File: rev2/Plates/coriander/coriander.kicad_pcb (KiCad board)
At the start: 2 copper layers, 242.9 x 88.2 mm, 44 parts

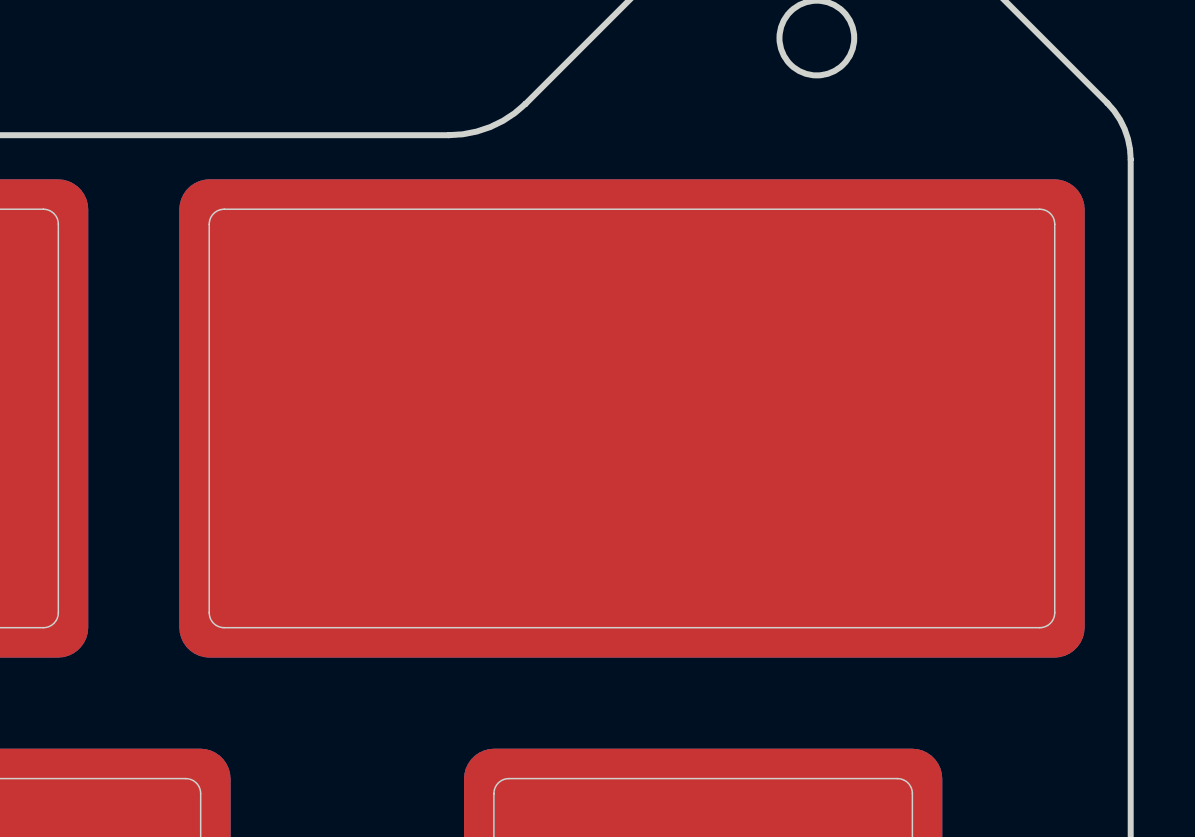
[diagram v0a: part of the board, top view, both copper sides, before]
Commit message: Fix plate encoder cutouts
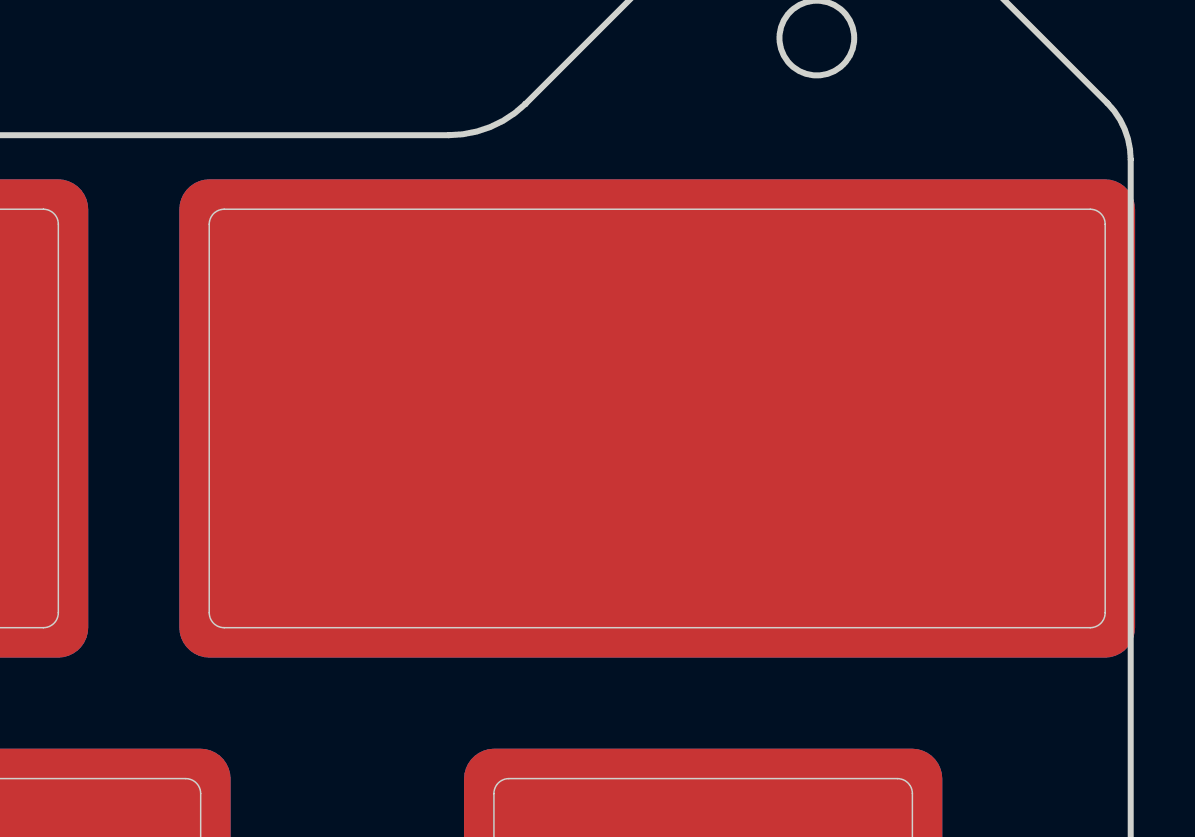
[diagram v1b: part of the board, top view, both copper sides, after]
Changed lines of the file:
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@@
     (visible_elements 7FFFEFFF)
     (pcbplotparams
-      (layerselection 0x01000_7ffffffe)
+      (layerselection 0x010c0_ffffffff)
       (usegerberextensions false)
       (usegerberattributes false)
@@
       (padsonsilk false)
       (subtractmaskfromsilk false)
-      (outputformat 3)
+      (outputformat 1)
       (mirror false)
       (drillshape 0)
@@
     (fp_line (start -16.66875 9.525) (end -16.66875 -9.525) (layer Dwgs.User) (width 0.15))
     (fp_line (start -16.66875 -9.525) (end 16.66875 -9.525) (layer Dwgs.User) (width 0.15))
-    (fp_line (start 13.64375 -7) (end -13.64375 -7) (layer Edge.Cuts) (width 0.05))
+    (fp_line (start 15.33125 -7) (end -13.64375 -7) (layer Edge.Cuts) (width 0.05))
     (fp_line (start -14.14375 -6.5) (end -14.14375 6.5) (layer Edge.Cuts) (width 0.05))
-    (fp_line (start -13.64375 7) (end 13.64375 7) (layer Edge.Cuts) (width 0.05))
-    (fp_line (start 14.14375 6.5) (end 14.14375 -6.5) (layer Edge.Cuts) (width 0.05))
-    (fp_arc (start 13.64375 -6.5) (end 14.14375 -6.5) (angle -90) (layer Edge.Cuts) (width 0.05))
+    (fp_line (start -13.64375 7) (end 15.33125 7) (layer Edge.Cuts) (width 0.05))
+    (fp_line (start 15.83125 6.5) (end 15.83125 -6.5) (layer Edge.Cuts) (width 0.05))
+    (fp_arc (start 15.33125 -6.5) (end 15.83125 -6.5) (angle -90) (layer Edge.Cuts) (width 0.05))
     (fp_arc (start -13.64375 -6.5) (end -13.64375 -7) (angle -90) (layer Edge.Cuts) (width 0.05))
     (fp_arc (start -13.64375 6.5) (end -14.14375 6.5) (angle -90) (layer Edge.Cuts) (width 0.05))
-    (fp_arc (start 13.64375 6.5) (end 13.64375 7) (angle -90) (layer Edge.Cuts) (width 0.05))
-    (pad 1 smd roundrect (at 0 0 180) (size 30.2875 16) (layers F.Cu F.Mask) (roundrect_rratio 0.063))
-    (pad 1 smd roundrect (at 0 0 180) (size 30.2875 16) (layers B.Cu B.Mask) (roundrect_rratio 0.063))
+    (fp_arc (start 15.33125 6.5) (end 15.33125 7) (angle -90) (layer Edge.Cuts) (width 0.05))
+    (pad 1 smd roundrect (at 0.84375 0 180) (size 31.975 16) (layers F.Cu F.Mask) (roundrect_rratio 0.063))
+    (pad 1 smd roundrect (at 0.84375 0 180) (size 31.975 16) (layers B.Cu B.Mask) (roundrect_rratio 0.063))
   )
   (module Keybage_MX_Cutout:MX_Cutout_3u (layer F.Cu)
